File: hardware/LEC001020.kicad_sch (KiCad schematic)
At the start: 11 parts

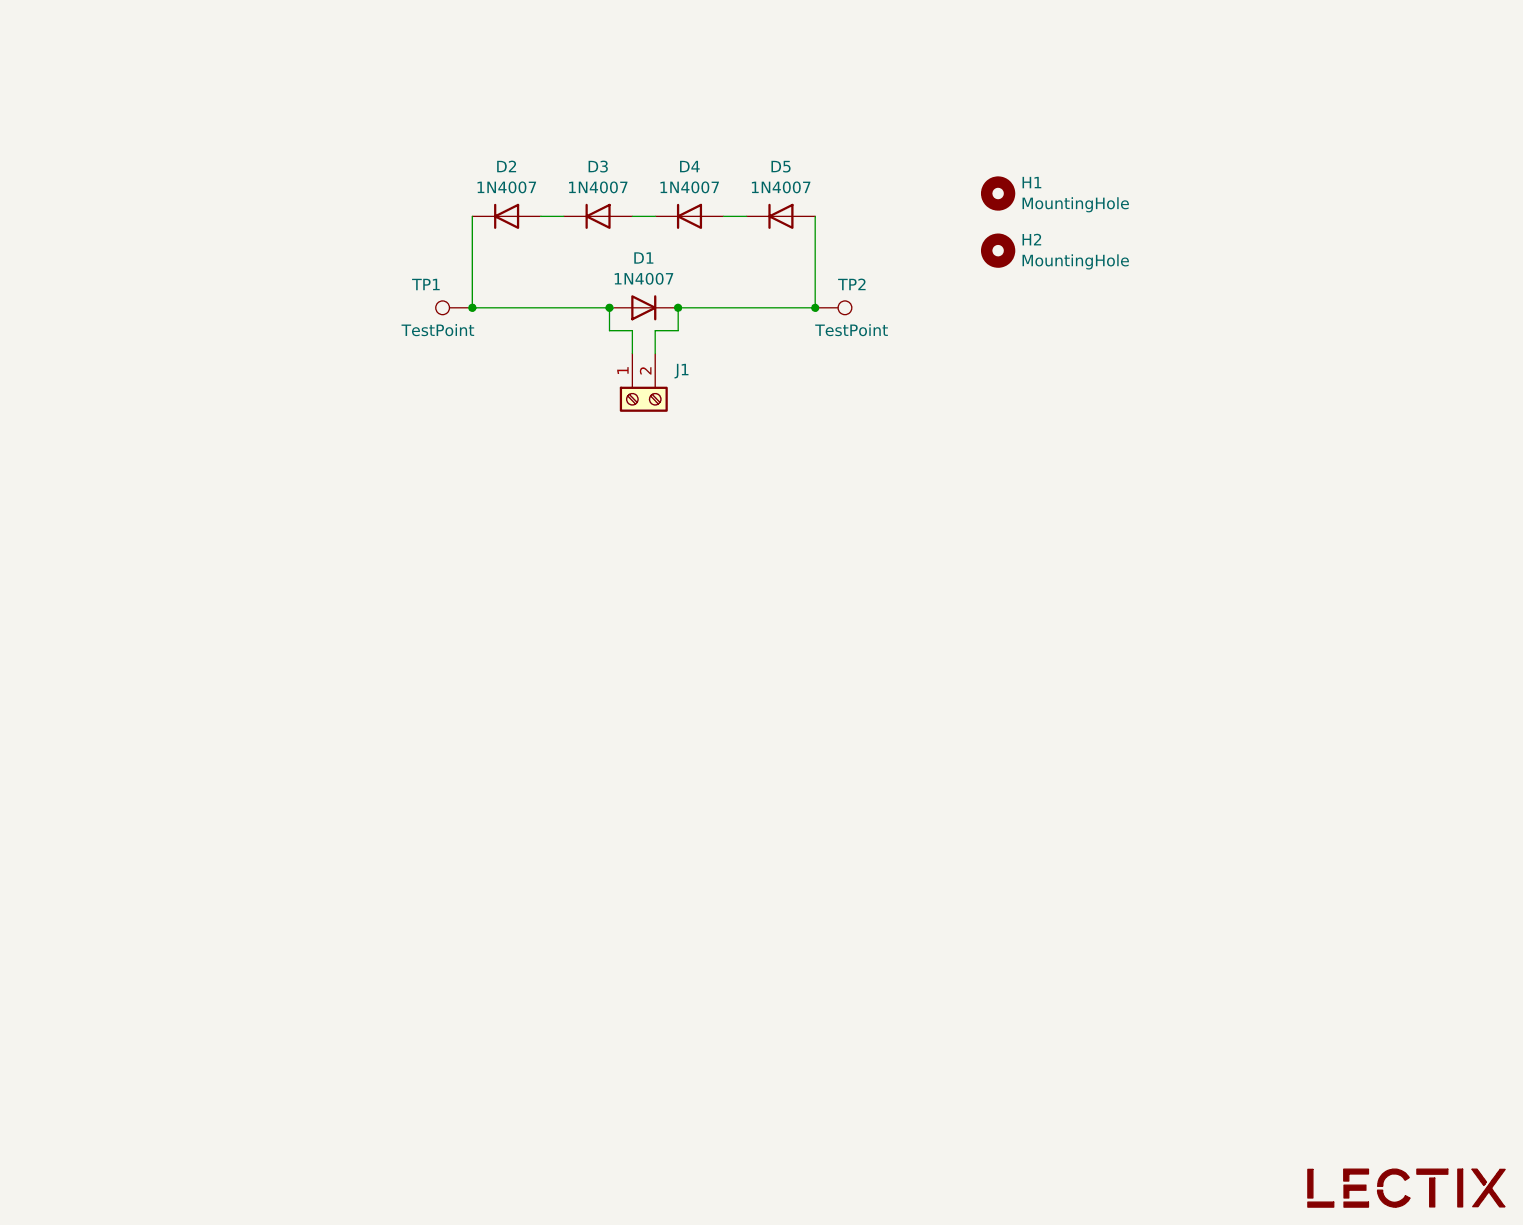
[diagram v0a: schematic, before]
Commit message: Update schematic sheet settings + add open hardware logo
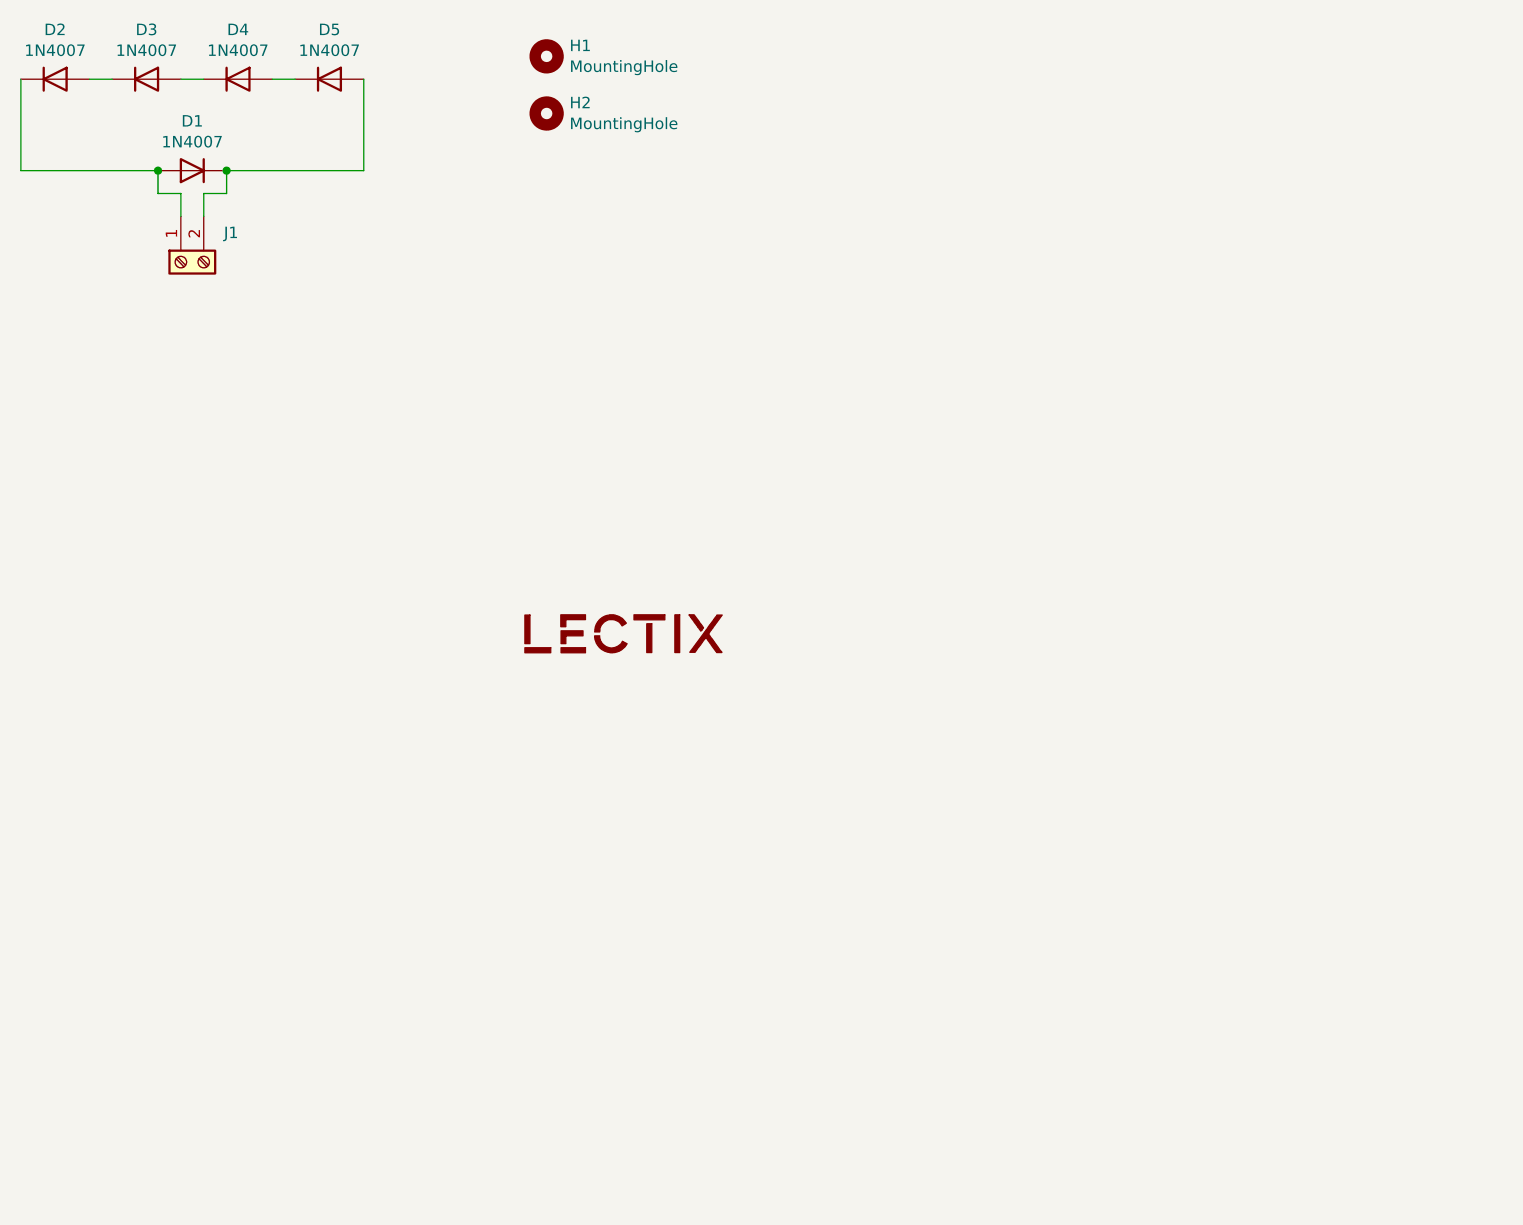
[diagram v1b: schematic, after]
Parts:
- removed TP1, TP2: TestPoint, TestPoint:TestPoint_THTPad_1.0x1.0mm_Drill0.5mm, symbol Connector:TestPoint
- J1: value (none) -> Screw_Terminal_01x02_blue; footprint (none) -> 0_connectors:TerminalBlock_bornier-2_P5.08mm-blue
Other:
- company: (none) -> LECTIX
- title: (none) -> LEC001020-Module-de-freinage-DCC-1A
- moved on the sheet: D1, D2, D3, D4, D5, H1, H2, J1

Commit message: Add prod files
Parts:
- J1: JLCPCB_CORRECTION (none) -> 2.54;0;180
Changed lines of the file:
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@@
+      (effects (font (size 1.27 1.27)) hide)
+    )
+    (property "JLCPCB_CORRECTION" "2.54;0;180" (id 8) (at 90.805 71.12 90)
       (effects (font (size 1.27 1.27)) hide)
     )
